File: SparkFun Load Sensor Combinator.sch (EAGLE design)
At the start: 14 parts

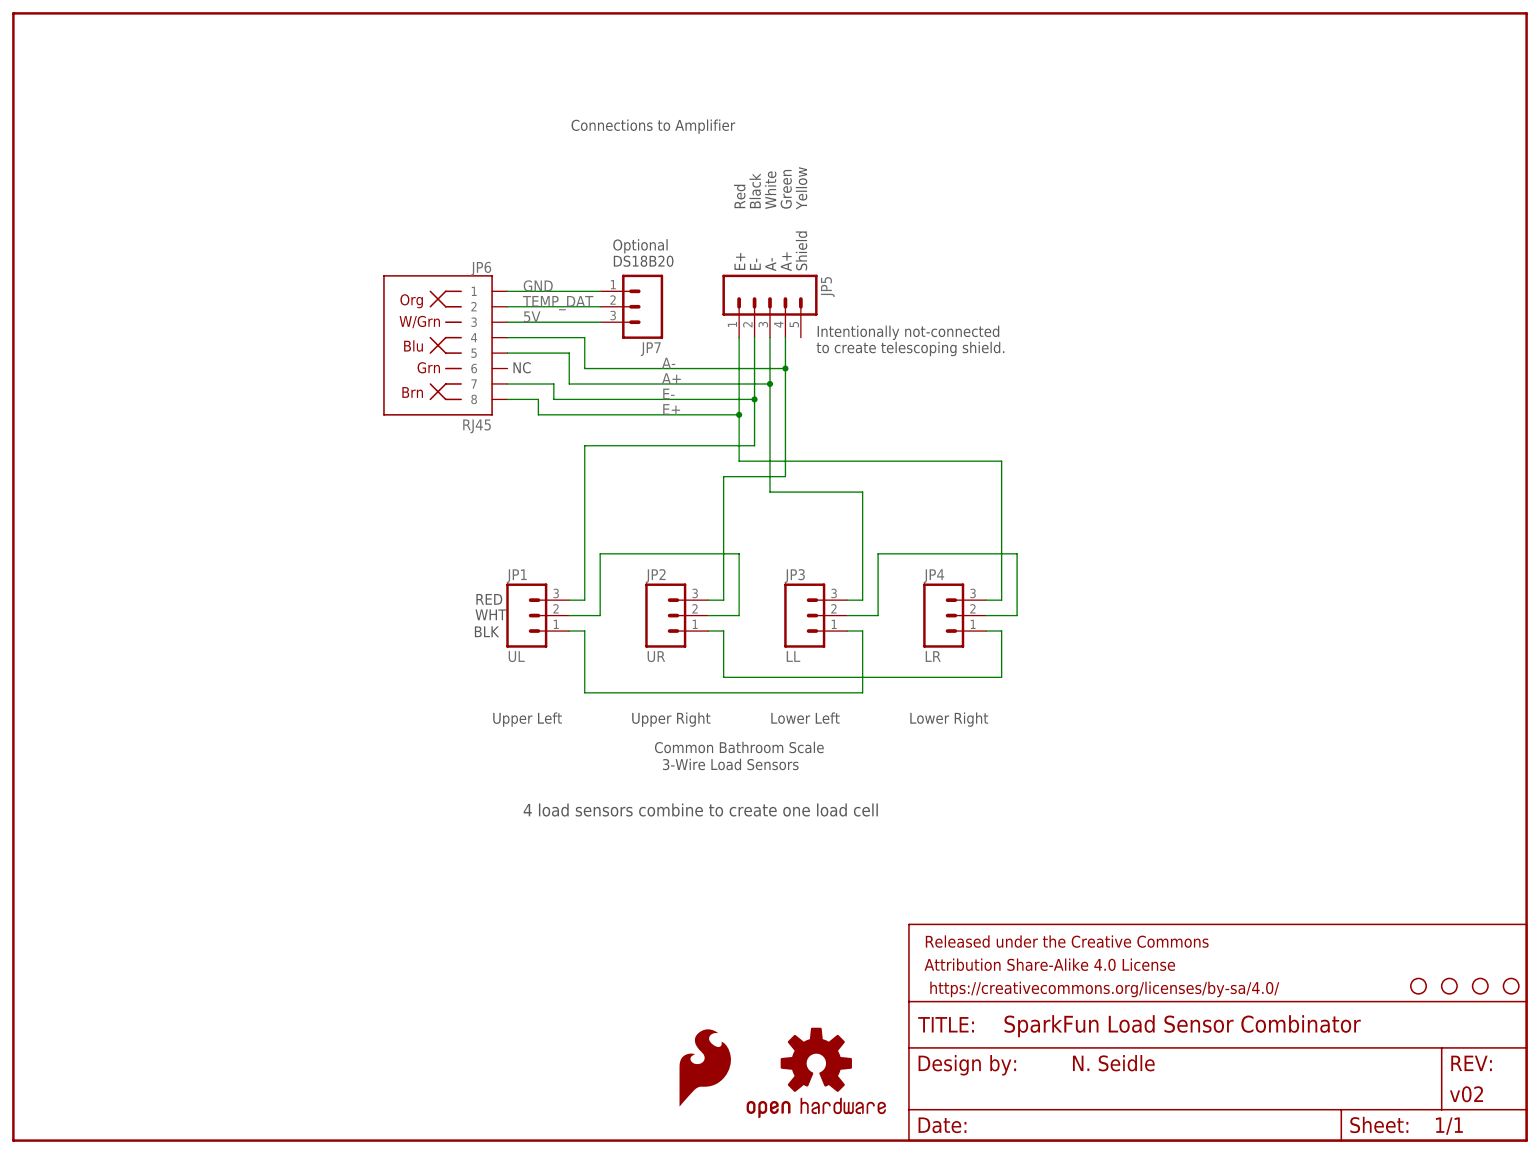
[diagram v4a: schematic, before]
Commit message: Fixed a swap between A+ and A-
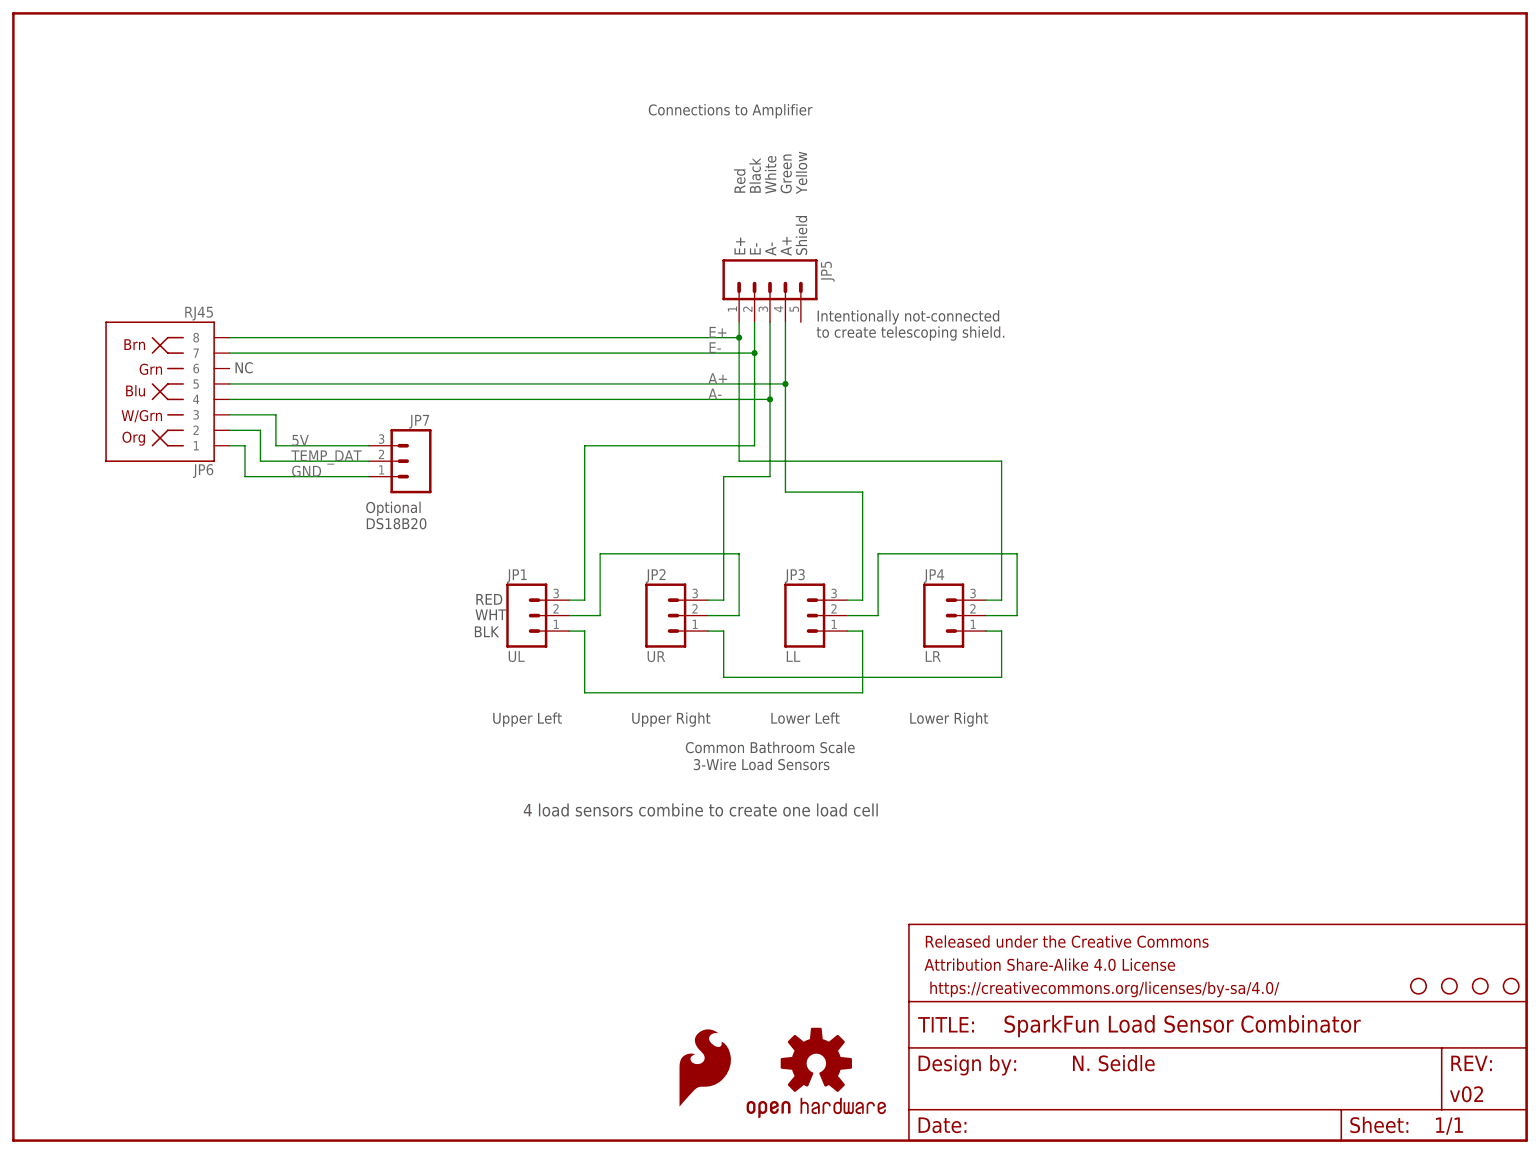
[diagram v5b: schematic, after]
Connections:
- net A+: now also JP5.4; no longer JP5.3
- net A-: now also JP5.3; no longer JP5.4
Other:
- moved on the sheet: JP5, JP6, JP7

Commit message: Update schematic version
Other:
- note added: "N. Seidle"
- note added: "v10"
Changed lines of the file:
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@@
 <?xml version="1.0" encoding="utf-8"?>
 <!DOCTYPE eagle SYSTEM "eagle.dtd">
-<eagle version="7.1.0">
+<eagle version="7.2.0">
 <drawing>
 <settings>
@@
 <layer number="56" name="wert" color="7" fill="1" visible="no" active="no"/>
 <layer number="57" name="tCAD" color="7" fill="1" visible="no" active="no"/>
+<layer number="59" name="tCarbon" color="7" fill="1" visible="no" active="no"/>
+<layer number="60" name="bCarbon" color="7" fill="1" visible="no" active="no"/>
 <layer number="90" name="Modules" color="5" fill="1" visible="yes" active="yes"/>
 <layer number="91" name="Nets" color="2" fill="1" visible="yes" active="yes"/>
@@
 <layer number="127" name="_tValues" color="7" fill="1" visible="yes" active="yes"/>
 <layer number="128" name="_bValues" color="7" fill="1" visible="yes" active="yes"/>
+<layer number="129" name="Mask" color="7" fill="1" visible="yes" active="yes"/>
 <layer number="131" name="tAdjust" color="7" fill="1" visible="yes" active="yes"/>
 <layer number="132" name="bAdjust" color="7" fill="1" visible="yes" active="yes"/>
@@
 <layer number="223" name="223bmp" color="24" fill="1" visible="no" active="no"/>
 <layer number="224" name="224bmp" color="25" fill="1" visible="no" active="no"/>
+<layer number="225" name="225bmp" color="7" fill="1" visible="yes" active="yes"/>
+<layer number="226" name="226bmp" color="7" fill="1" visible="yes" active="yes"/>
+<layer number="227" name="227bmp" color="7" fill="1" visible="yes" active="yes"/>
+<layer number="228" name="228bmp" color="7" fill="1" visible="yes" active="yes"/>
+<layer number="229" name="229bmp" color="7" fill="1" visible="yes" active="yes"/>
+<layer number="230" name="230bmp" color="7" fill="1" visible="yes" active="yes"/>
+<layer number="231" name="231bmp" color="7" fill="1" visible="yes" active="yes"/>
 <layer number="248" name="Housing" color="7" fill="1" visible="yes" active="yes"/>
 <layer number="249" name="Edge" color="7" fill="1" visible="yes" active="yes"/>
@@
 <layer number="251" name="SMDround" color="12" fill="11" visible="no" active="no"/>
 <layer number="254" name="cooling" color="7" fill="1" visible="no" active="yes"/>
+<layer number="255" name="routoute" color="7" fill="1" visible="yes" active="yes"/>
 </layers>
 <schematic xreflabel="%F%N/%S" xrefpart="/%S.%C%R">
@@
 <text x="57.912" y="100.584" size="1.778" layer="97">Optional
 DS18B20</text>
+<text x="170.942" y="11.43" size="2.54" layer="94">N. Seidle</text>
+<text x="238.76" y="7.62" size="2.54" layer="94">v10</text>
 </plain>
 <instances>

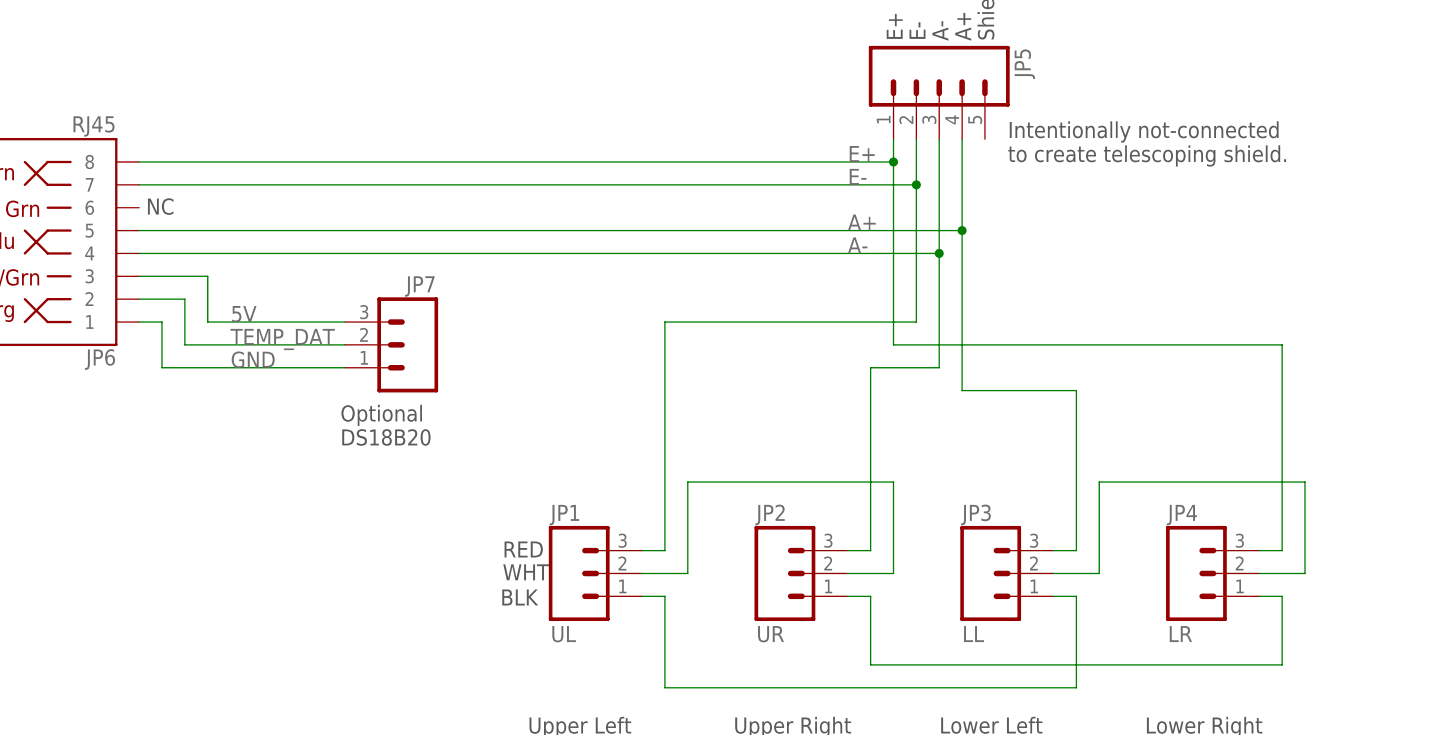
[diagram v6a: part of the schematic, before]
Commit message: Adding 5V and GND symbols to schematic.
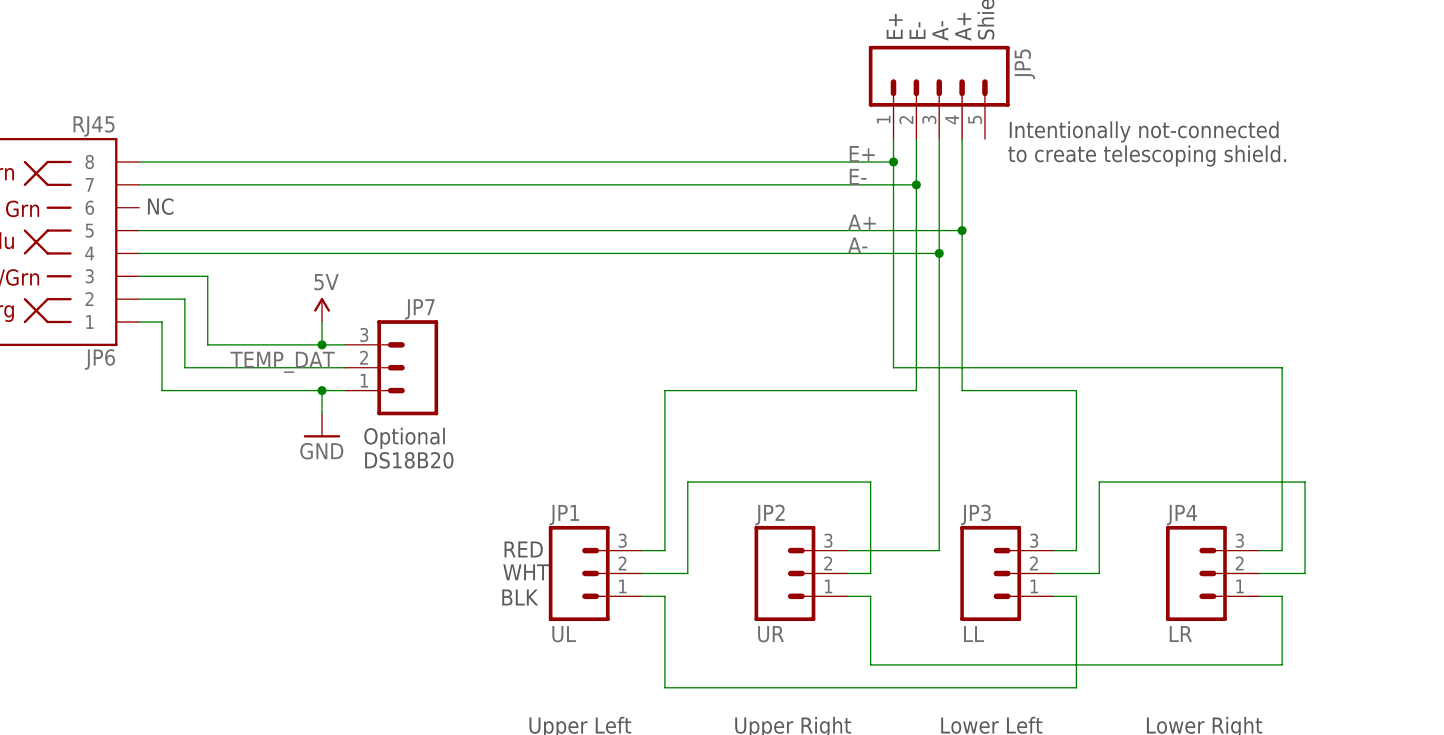
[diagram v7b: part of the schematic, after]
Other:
- moved on the sheet: JP7
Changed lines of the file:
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@@
 <part name="JP6" library="SparkFun-Connectors" deviceset="RJ45-8" device="PTH" value="RJ45"/>
 <part name="JP7" library="SparkFun-Connectors" deviceset="M03" device="PTH"/>
+<part name="GND1" library="SparkFun-Aesthetics" deviceset="GND" device=""/>
+<part name="SUPPLY1" library="SparkFun-Aesthetics" deviceset="5V" device=""/>
 </parts>
 <sheets>
@@
 to create telescoping shield.</text>
 <text x="36.322" y="126.238" size="1.778" layer="97">NC</text>
-<text x="57.912" y="100.584" size="1.778" layer="97">Optional
+<text x="60.452" y="98.044" size="1.778" layer="97">Optional
 DS18B20</text>
 <text x="170.942" y="11.43" size="2.54" layer="94">N. Seidle</text>
@@
 <instance part="JP5" gate="G$1" x="124.46" y="142.24" rot="R270"/>
 <instance part="JP6" gate="JP1" x="27.94" y="121.92" rot="R180"/>
-<instance part="JP7" gate="G$1" x="66.04" y="111.76" rot="MR0"/>
+<instance part="JP7" gate="G$1" x="66.04" y="109.22" rot="MR0"/>
+<instance part="GND1" gate="1" x="55.88" y="101.6"/>
+<instance part="SUPPLY1" gate="G$1" x="55.88" y="114.3"/>
 </instances>
 <busses>
@@
 <segment>
 <pinref part="JP2" gate="G$1" pin="2"/>
-<wire x1="114.3" y1="86.36" x2="119.38" y2="86.36" width="0.1524" layer="91"/>
-<wire x1="119.38" y1="86.36" x2="119.38" y2="96.52" width="0.1524" layer="91"/>
-<wire x1="119.38" y1="96.52" x2="96.52" y2="96.52" width="0.1524" layer="91"/>
+<wire x1="114.3" y1="86.36" x2="116.84" y2="86.36" width="0.1524" layer="91"/>
+<wire x1="116.84" y1="86.36" x2="116.84" y2="96.52" width="0.1524" layer="91"/>
+<wire x1="116.84" y1="96.52" x2="96.52" y2="96.52" width="0.1524" layer="91"/>
 <wire x1="96.52" y1="96.52" x2="96.52" y2="86.36" width="0.1524" layer="91"/>
 <pinref part="JP1" gate="G$1" pin="2"/>
@@
 <pinref part="JP4" gate="G$1" pin="3"/>
 <wire x1="160.02" y1="88.9" x2="162.56" y2="88.9" width="0.1524" layer="91"/>
-<wire x1="162.56" y1="88.9" x2="162.56" y2="111.76" width="0.1524" layer="91"/>
-<wire x1="119.38" y1="111.76" x2="162.56" y2="111.76" width="0.1524" layer="91"/>
-<wire x1="119.38" y1="111.76" x2="119.38" y2="132.08" width="0.1524" layer="91"/>
+<wire x1="162.56" y1="88.9" x2="162.56" y2="109.22" width="0.1524" layer="91"/>
+<wire x1="119.38" y1="109.22" x2="162.56" y2="109.22" width="0.1524" layer="91"/>
+<wire x1="119.38" y1="109.22" x2="119.38" y2="132.08" width="0.1524" layer="91"/>
 <pinref part="JP5" gate="G$1" pin="1"/>
 <wire x1="119.38" y1="132.08" x2="119.38" y2="134.62" width="0.1524" layer="91"/>
@@
 <segment>
 <pinref part="JP2" gate="G$1" pin="3"/>
-<wire x1="114.3" y1="88.9" x2="116.84" y2="88.9" width="0.1524" layer="91"/>
-<wire x1="116.84" y1="88.9" x2="116.84" y2="109.22" width="0.1524" layer="91"/>
-<wire x1="116.84" y1="109.22" x2="124.46" y2="109.22" width="0.1524" layer="91"/>
-<wire x1="124.46" y1="121.92" x2="124.46" y2="109.22" width="0.1524" layer="91"/>
+<wire x1="114.3" y1="88.9" x2="124.46" y2="88.9" width="0.1524" layer="91"/>
+<wire x1="124.46" y1="88.9" x2="124.46" y2="121.92" width="0.1524" layer="91"/>
 <wire x1="124.46" y1="121.92" x2="35.56" y2="121.92" width="0.1524" layer="91"/>
 <pinref part="JP6" gate="JP1" pin="4"/>
@@
 <net name="E-" class="0">
 <segment>
-<wire x1="121.92" y1="114.3" x2="121.92" y2="129.54" width="0.1524" layer="91"/>
+<wire x1="121.92" y1="106.68" x2="121.92" y2="129.54" width="0.1524" layer="91"/>
 <wire x1="121.92" y1="129.54" x2="121.92" y2="134.62" width="0.1524" layer="91"/>
-<wire x1="121.92" y1="114.3" x2="93.98" y2="114.3" width="0.1524" layer="91"/>
-<wire x1="93.98" y1="114.3" x2="93.98" y2="88.9" width="0.1524" layer="91"/>
+<wire x1="121.92" y1="106.68" x2="93.98" y2="106.68" width="0.1524" layer="91"/>
+<wire x1="93.98" y1="106.68" x2="93.98" y2="88.9" width="0.1524" layer="91"/>
 <pinref part="JP1" gate="G$1" pin="3"/>
 <wire x1="93.98" y1="88.9" x2="91.44" y2="88.9" width="0.1524" layer="91"/>
@@
 <pinref part="JP7" gate="G$1" pin="3"/>
 <wire x1="35.56" y1="119.38" x2="43.18" y2="119.38" width="0.1524" layer="91"/>
-<wire x1="43.18" y1="119.38" x2="43.18" y2="114.3" width="0.1524" layer="91"/>
-<wire x1="43.18" y1="114.3" x2="58.42" y2="114.3" width="0.1524" layer="91"/>
-<label x="45.72" y="114.3" size="1.778" layer="95"/>
+<wire x1="43.18" y1="119.38" x2="43.18" y2="111.76" width="0.1524" layer="91"/>
+<wire x1="43.18" y1="111.76" x2="55.88" y2="111.76" width="0.1524" layer="91"/>
+<pinref part="SUPPLY1" gate="G$1" pin="5V"/>
+<wire x1="55.88" y1="111.76" x2="58.42" y2="111.76" width="0.1524" layer="91"/>
+<wire x1="55.88" y1="114.3" x2="55.88" y2="111.76" width="0.1524" layer="91"/>
+<junction x="55.88" y="111.76"/>
 </segment>
 </net>
@@
 <pinref part="JP7" gate="G$1" pin="2"/>
 <wire x1="35.56" y1="116.84" x2="40.64" y2="116.84" width="0.1524" layer="91"/>
-<wire x1="40.64" y1="116.84" x2="40.64" y2="111.76" width="0.1524" layer="91"/>
-<wire x1="40.64" y1="111.76" x2="58.42" y2="111.76" width="0.1524" layer="91"/>
-<label x="45.72" y="111.76" size="1.778" layer="95"/>
+<wire x1="40.64" y1="116.84" x2="40.64" y2="109.22" width="0.1524" layer="91"/>
+<wire x1="40.64" y1="109.22" x2="58.42" y2="109.22" width="0.1524" layer="91"/>
+<label x="45.72" y="109.22" size="1.778" layer="95"/>
 </segment>
 </net>
@@
 <pinref part="JP7" gate="G$1" pin="1"/>
 <wire x1="35.56" y1="114.3" x2="38.1" y2="114.3" width="0.1524" layer="91"/>
-<wire x1="38.1" y1="114.3" x2="38.1" y2="109.22" width="0.1524" layer="91"/>
-<wire x1="38.1" y1="109.22" x2="58.42" y2="109.22" width="0.1524" layer="91"/>
-<label x="45.72" y="109.22" size="1.778" layer="95"/>
-</segment>
-</net>
+<wire x1="38.1" y1="114.3" x2="38.1" y2="106.68" width="0.1524" layer="91"/>
+<wire x1="38.1" y1="106.68" x2="55.88" y2="106.68" width="0.1524" layer="91"/>
+<pinref part="GND1" gate="1" pin="GND"/>
+<wire x1="55.88" y1="106.68" x2="58.42" y2="106.68" width="0.1524" layer="91"/>
+<wire x1="55.88" y1="106.68" x2="55.88" y2="104.14" width="0.1524" layer="91"/>
+<junction x="55.88" y="106.68"/>
+</segment>
+</net>
